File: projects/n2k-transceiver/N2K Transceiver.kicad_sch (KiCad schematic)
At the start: 131 parts, among them SW1 TS03-66-50-BK-160-LCR-D-67, SW2 TS03-66-50-BK-160-LCR-D-67, SW3 TS03-66-50-BK-160-LCR-D-67

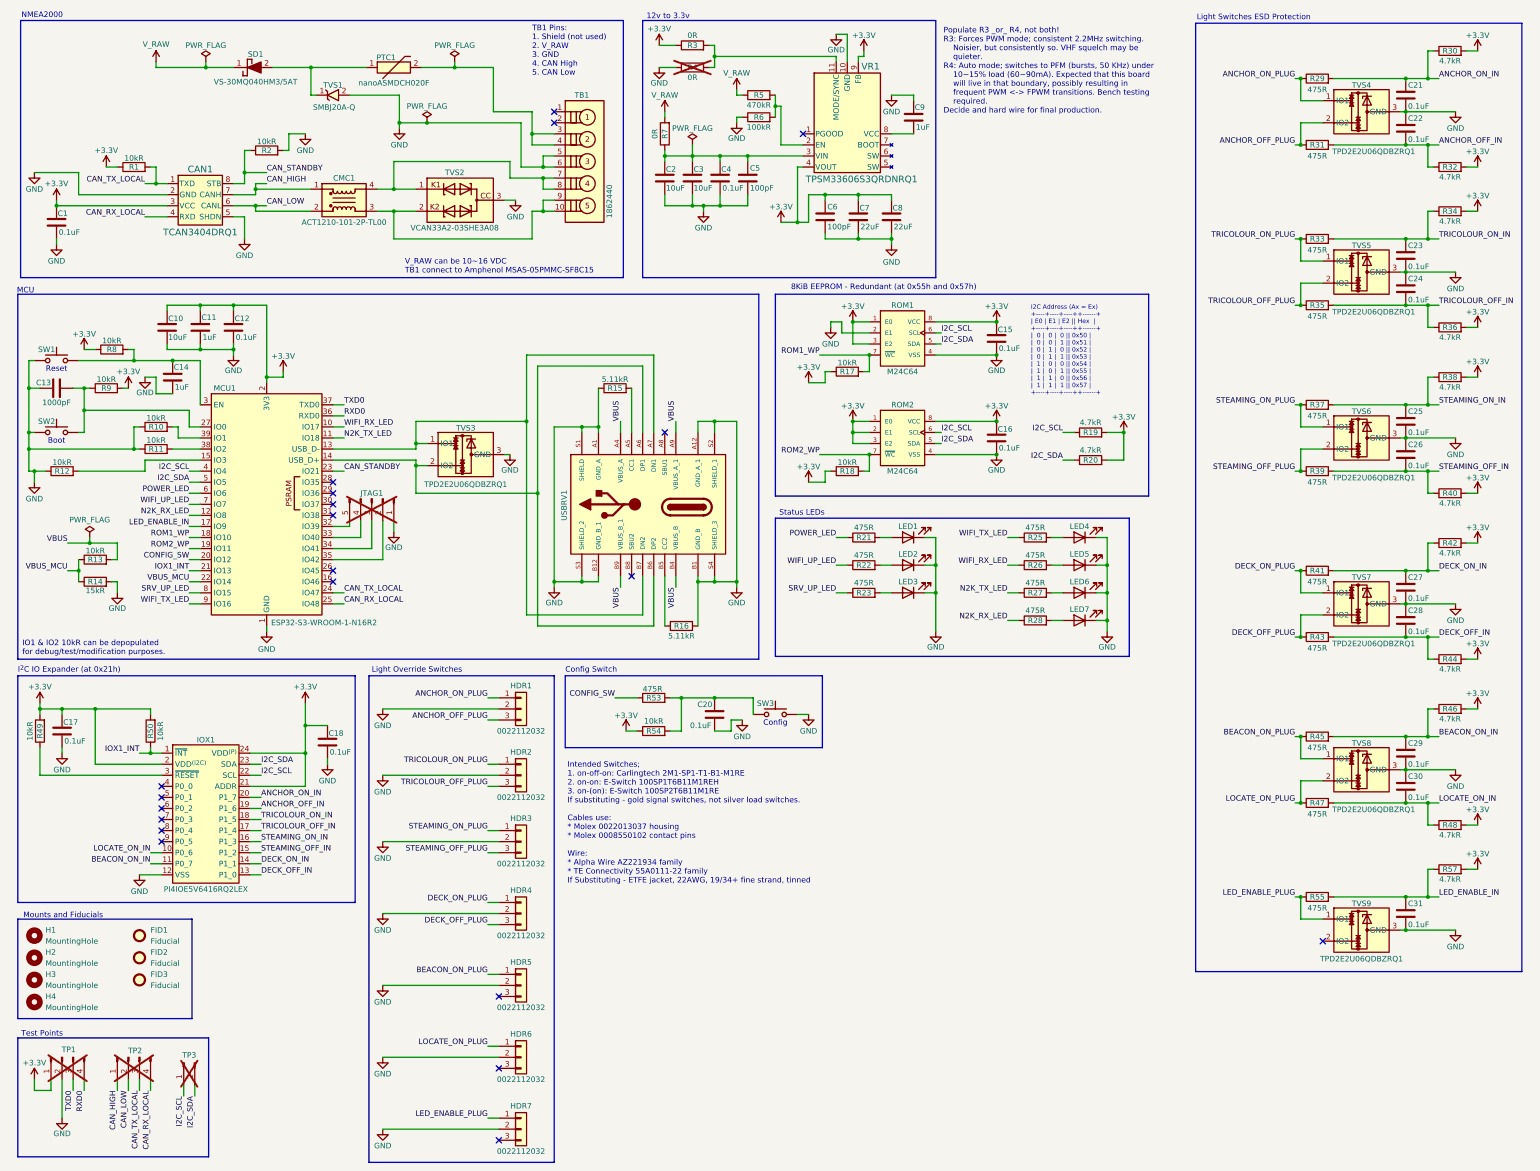
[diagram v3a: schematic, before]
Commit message: Working on switching the IOX1 to the SMI1 switch chip.
Signed-off-by: digimer <digital.mermaid@gmail.com>
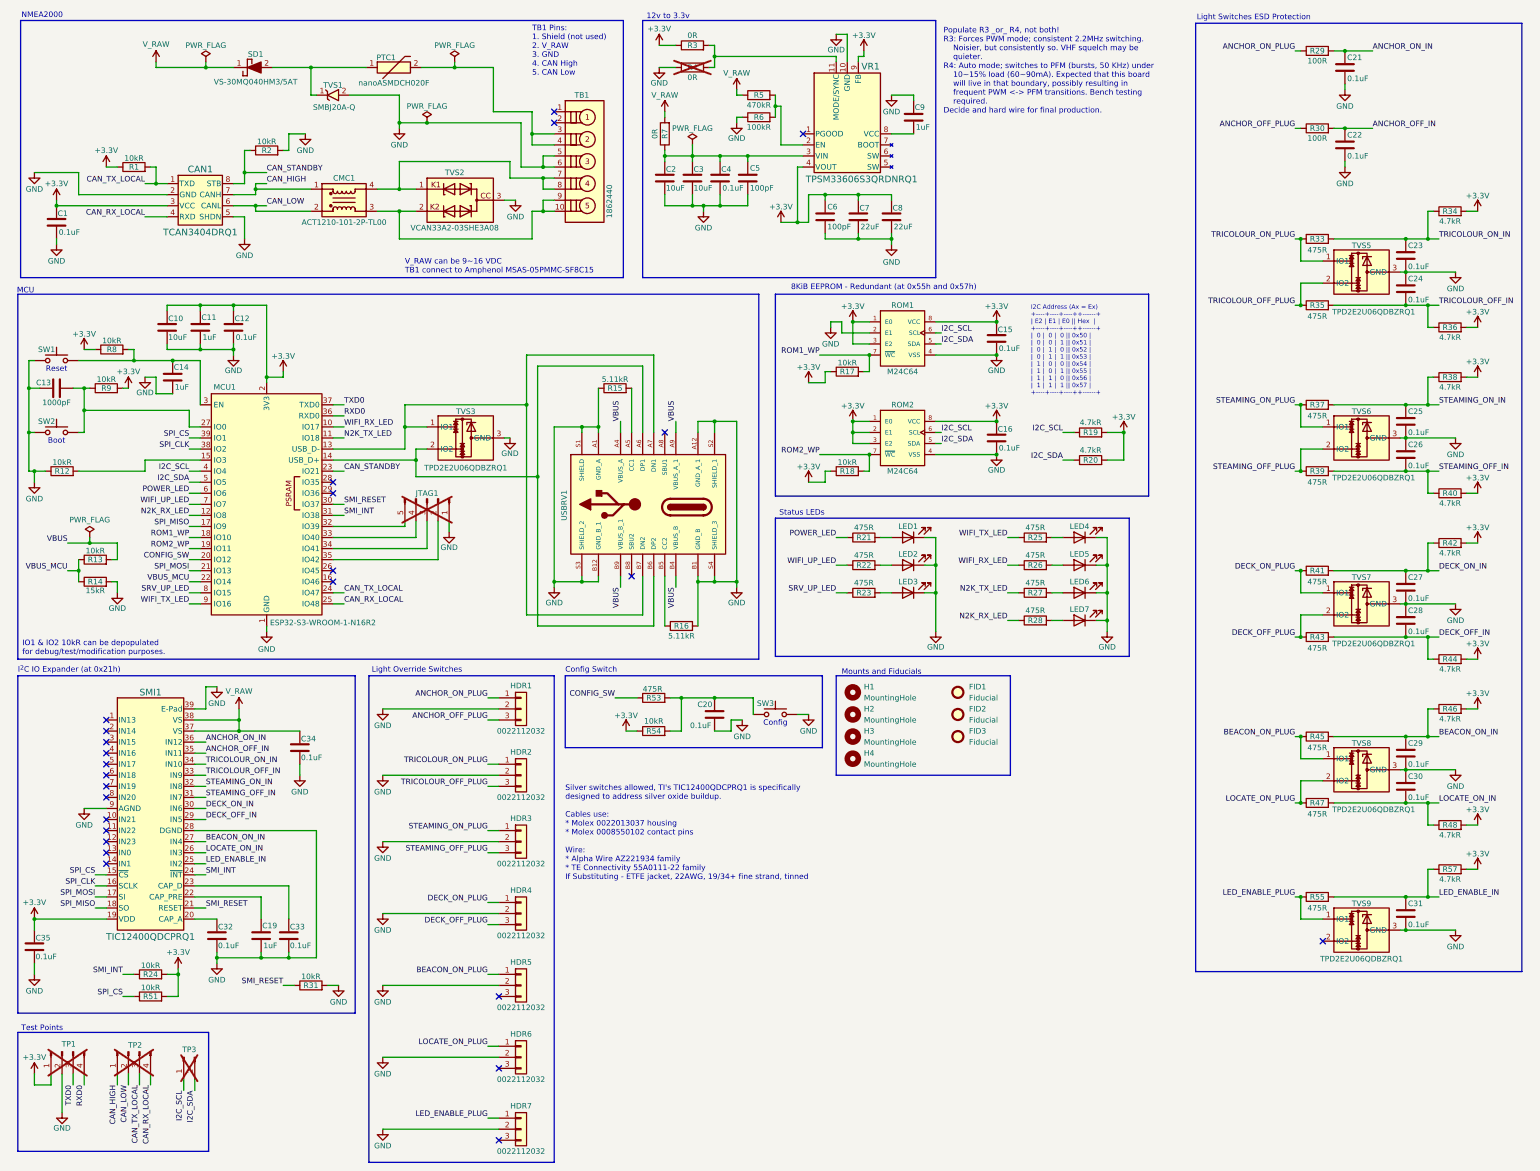
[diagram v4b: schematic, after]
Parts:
- removed C17, C18: 0.1uF, mr-stuff:Kyocera AVX 0805, symbol mr-parts:Kyocera 08051C104K4Z2A
- removed IOX1: PI4IOE5V6416RQ2LEX, mr-stuff:Diodes Inc PI4IOE5V6416RQ2LEX, symbol mr-parts:Diodes Inc PI4IOE5V6416RQ2LEX
- removed MCU1: ESP32-S3-WROOM-1-N16R2, RF_Module:ESP32-S3-WROOM-1, symbol RF_Module:ESP32-S3-WROOM-1
- removed R10, R11, R49, R50: 10kR, mr-stuff:Stackpole RNCP0805, symbol mr-parts:Stackpole RNCP0805FTD10K0
- removed R29, R31: 475R, mr-stuff:Stackpole RNCP0805, symbol mr-parts:Stackpole RNCP0805FTD475R
- removed R30, R32: 4.7kR, mr-stuff:Stackpole RMCA0805, symbol mr-parts:Stackpole RMCA0805FT4K70-HP
- removed TVS4: TPD2E2U06QDBZRQ1, mr-stuff:TI TPD2E2U06, symbol mr-parts:TVS TPD2E2U06QDBZRQ1
- added C19: 1uF, mr-stuff:Kyocera AVX 0805, symbol mr-parts:Kyocera 08051C105K4Z2A
- added C32, C33, C34, C35: 0.1uF, mr-stuff:Kyocera AVX 0805, symbol mr-parts:Kyocera 08051C104K4Z2A
- added MCU1: ESP32-S3-WROOM-1-N16R2, mr-stuff:Espressif ESP32-S3, symbol mr-parts:Espressif ESP32-S3-WROOM-1-N16R2
- added R24, R31, R51: 10kR, mr-stuff:Stackpole RNCP0805, symbol mr-parts:Stackpole RNCP0805FTD10K0
- added R29, R30: 100R, mr-stuff:Stackpole RNCP0805, symbol mr-parts:Stackpole RNCP0805FTD100R
- added SMI1: TIC12400QDCPRQ1, mr-stuff:TI TIC12400QDCPRQ1, symbol mr-parts:TI TIC12400QDCPRQ1
- C1, C12, C15, C16, C20, C21, C22, C23, C24, C25, C26, C27, C28, C29, C30, C31, C4: Datasheet2 (none) -> https://spicat.kyocera-avx.com/datasheet/08051C104K4Z2A
- C11, C14, C9: Datasheet2 (none) -> https://spicat.kyocera-avx.com/datasheet/08051C105K4Z2A
- CMC1: symbol mr-parts:TDK ACT1210-510-2P-TL00 -> mr-parts:TDK ACT1210-101-2P-TL00
- SD1: symbol mr-parts:Vishay VS-30MQ040-M3_5AT -> mr-parts:Vishay VS-30MQ040HM3/5AT
- TVS1: symbol mr-parts:Bouns SMBJ20A-Q -> mr-parts:Bourns SMBJ20A-Q
- TVS3, TVS5, TVS6, TVS7, TVS8, TVS9: symbol mr-parts:TVS TPD2E2U06QDBZRQ1 -> mr-parts:TI TPD2E2U06QDBZRQ1
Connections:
- net +3.3V: now also C35.1, MCU1.2 (3V3), R24.2, R51.2, SMI1.19 (VDD)
- net ANCHOR_OFF_IN: now also C22.1, R30.2, SMI1.35 (IN11); no longer C22.2
- net ANCHOR_OFF_PLUG: now also R30.1
- net ANCHOR_ON_IN: now also R29.2, SMI1.36 (IN12)
- net ANCHOR_ON_PLUG: now also R29.1
- net BEACON_ON_IN: now also SMI1.27 (IN4)
- net CAN_RX_LOCAL: now also MCU1.25 (IO48)
- net CAN_STANDBY: now also MCU1.23 (IO21)
- net CAN_TX_LOCAL: now also MCU1.24 (IO47)
- net CONFIG_SW: now also MCU1.20 (IO12)
- net DECK_OFF_IN: now also SMI1.29 (IN5)
- net DECK_ON_IN: now also SMI1.30 (IN6)
- net GND: now also C22.2, C19.2, C32.2, C33.2, C34.2, C35.2, MCU1.1 (GND), MCU1.40 (GND), MCU1.41 (GND), R31.2, SMI1.28 (DGND), SMI1.39 (E-Pad), SMI1.9 (AGND); no longer C22.1
- net I2C_SCL: now also MCU1.4 (IO4)
- net I2C_SDA: now also MCU1.5 (IO5)
- net LED_ENABLE_IN: now also SMI1.25 (IN2)
- net LOCATE_ON_IN: now also SMI1.26 (IN3)
- net N2K_RX_LED: now also MCU1.12 (IO8)
- net N2K_TX_LED: now also MCU1.11 (IO18)
- net POWER_LED: now also MCU1.6 (IO6)
- net ROM1_WP: now also MCU1.18 (IO10)
- net ROM2_WP: now also MCU1.19 (IO11)
- net RXD0: now also MCU1.36 (RXD0)
- net SRV_UP_LED: now also MCU1.8 (IO15)
- net STEAMING_OFF_IN: now also SMI1.31 (IN7)
- net STEAMING_ON_IN: now also SMI1.32 (IN8)
- net TRICOLOUR_OFF_IN: now also SMI1.33 (IN9)
- net TRICOLOUR_ON_IN: now also SMI1.34 (IN10)
- net TXD0: now also MCU1.37 (TXD0)
- net VBUS_MCU: now also MCU1.22 (IO14)
- net V_RAW: now also C34.1, SMI1.37 (VS), SMI1.38 (VS)
- net WIFI_RX_LED: now also MCU1.10 (IO17)
- net WIFI_TX_LED: now also MCU1.9 (IO16)
- net WIFI_UP_LED: now also MCU1.7 (IO7)
- net at C13.2, R9.1, SW2.3 (B)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: now also MCU1.27 (IO0)
- net at C14.1, R8.2, SW1.3 (B)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: now also MCU1.3 (EN)
- net at JTAG1.2 (Pin_2): now also MCU1.35 (IO42)
- net at JTAG1.3 (Pin_3): now also MCU1.34 (IO41)
- net at JTAG1.4 (Pin_4): now also MCU1.33 (IO40)
- net at JTAG1.5 (Pin_5): now also MCU1.32 (IO39)
- net at R12.2: now also MCU1.15 (IO3)
- net at TVS3.1 (IO1), USBRV1.A7 (DN1), USBRV1.B7 (DN2): now also MCU1.13 (USB_D-)
- net at TVS3.2 (IO2), USBRV1.A6 (DP1), USBRV1.B6 (DP2): now also MCU1.14 (USB_D+)
- new net: C19.1, SMI1.22 (CAP_PRE)
- new net: C32.1, SMI1.20 (CAP_A)
- new net: C33.1, SMI1.23 (CAP_D)
- new net SMI_INT: MCU1.31 (IO38), R24.1, SMI1.24 (~{INT})
- new net SMI_RESET: MCU1.30 (IO37), R31.1, SMI1.21 (RESET)
- new net SPI_CLK: MCU1.38 (IO2), SMI1.16 (SCLK)
- new net SPI_CS: MCU1.39 (IO1), R51.1, SMI1.15 (~{CS})
- new net SPI_MISO: MCU1.17 (IO9), SMI1.18 (SO)
- new net SPI_MOSI: MCU1.21 (IO13), SMI1.17 (SI)
- no-connect marks 21 -> 26
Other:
- note added: "I2C Address (Ax = Ex) +----+----+----++------+ | E2 | E1 | E0 || Hex | +----+----+----++------+ | 0 | 0 | 0 || 0x50 | | 0 | 0 | 1 || 0x51 | | 0 | 1 | 0 || 0x52 | | 0 | 1 | 1 || 0x53 | | 1 | 0 | 0 || 0x54 | | 1 | 0 | 1 || 0x55 | | 1 | 1 | 0 || 0x56 | | 1 | 1 | 1 || 0x57 | +----+----+----++------+"
- note added: "Populate R3 _or_ R4, not both! R3: Forces PWM mode; consistent 2.2MHz switching. Noisier, but consistently so. VHF squelch may be quieter. R4: Auto mode; switches to PFM (bursts, 50 KHz) under 10~15% load (60~90mA). Expected that this board will live in that boundary, possibly resulting in frequent PWM <-> PFM transitions. Bench testing required. Decide and hard wire for final production."
- note added: "Silver switches allowed, TI's TIC12400QDCPRQ1 is specifically designed to address silver oxide buildup. Cables use: * Molex 0022013037 housing * Molex 0008550102 contact pins Wire: * Alpha Wire AZ221934 family * TE Connectivity 55A0111-22 family If Substituting - ETFE jacket, 22AWG, 19/34+ fine strand, tinned"
- note added: "V_RAW can be 9~16 VDC TB1 connect to Amphenol MSAS-05PMMC-SF8C15"
- note removed: "I2C Address (Ax = Ex) +----+----+----++------+ | E0 | E1 | E2 || Hex | +----+----+----++------+ | 0 | 0 | 0 || 0x50 | | 0 | 0 | 1 || 0x51 | | 0 | 1 | 0 || 0x52 | | 0 | 1 | 1 || 0x53 | | 1 | 0 | 0 || 0x54 | | 1 | 0 | 1 || 0x55 | | 1 | 1 | 0 || 0x56 | | 1 | 1 | 1 || 0x57 | +----+----+----++------+"
- note removed: "Intended Switches; 1. on-off-on: Carlingtech 2M1-SP1-T1-B1-M1RE 2. on-on: E-Switch 100SP1T6B11M1REH 3. on-(on): E-Switch 100SP2T6B11M1RE If substituting - gold signal switches, not silver load switches. Cables use: * Molex 0022013037 housing * Molex 0008550102 contact pins Wire: * Alpha Wire AZ221934 family * TE Connectivity 55A0111-22 family If Substituting - ETFE jacket, 22AWG, 19/34+ fine stra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"
- note removed: "Populate R3 _or_ R4, not both! R3: Forces PWM mode; consistent 2.2MHz switching. Noisier, but consistently so. VHF squelch may be quieter. R4: Auto mode; switches to PFM (bursts, 50 KHz) under 10~15% load (60~90mA). Expected that this board will live in that boundary, possibly resulting in frequent PWM <-> FPWM transitions. Bench testing required. Decide and hard wire for final production."
- note removed: "V_RAW can be 10~16 VDC TB1 connect to Amphenol MSAS-05PMMC-SF8C15"
- moved on the sheet: C21, C22, FID1, FID2, FID3, H1, H2, H3, H4, JTAG1, TP1, TP2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

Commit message: Finished the schematic update to use the SMI1.
Also updated the ESD protection to account for the TIC12400QDCPRQ1's internal ESD functions.

Signed-off-by: digimer <digital.mermaid@gmail.com>
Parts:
- removed C23, C24, C25, C26, C27, C28, C29, C30, C31: 0.1uF, mr-stuff:Kyocera AVX 0805, symbol mr-parts:Kyocera 08051C104K4Z2A
- removed R33, R35, R37, R39, R41, R43, R45, R47, R55: 475R, mr-stuff:Stackpole RNCP0805, symbol mr-parts:Stackpole RNCP0805FTD475R
- removed R34, R36, R38, R40, R42, R44, R46, R48, R57: 4.7kR, mr-stuff:Stackpole RMCA0805, symbol mr-parts:Stackpole RMCA0805FT4K70-HP
- removed TVS5, TVS6, TVS7, TVS8, TVS9: TPD2E2U06QDBZRQ1, mr-stuff:TI TPD2E2U06, symbol mr-parts:TI TPD2E2U06QDBZRQ1
- added C36, C37, C38, C39, C40, C41, C42, C43, C44: 0.1uF, mr-stuff:Kyocera AVX 0805, symbol mr-parts:Kyocera 08051C104K4Z2A
- added R33, R35, R37, R39, R41, R43, R45, R47, R55: 100R, mr-stuff:Stackpole RNCP0805, symbol mr-parts:Stackpole RNCP0805FTD100R
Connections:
- net BEACON_ON_IN: now also C42.1, R45.2
- net BEACON_ON_PLUG: now also R45.1
- net DECK_OFF_IN: now also C41.1, R43.2
- net DECK_OFF_PLUG: now also R43.1
- net DECK_ON_IN: now also C40.1, R41.2
- net DECK_ON_PLUG: now also R41.1
- net GND: now also C36.2, C37.2, C38.2, C39.2, C40.2, C41.2, C42.2, C43.2, C44.2
- net LED_ENABLE_IN: now also C44.1, R55.2
- net LED_ENABLE_PLUG: now also R55.1
- net LOCATE_ON_IN: now also C43.1, R47.2
- net LOCATE_ON_PLUG: now also R47.1
- net STEAMING_OFF_IN: now also C39.1, R39.2
- net STEAMING_OFF_PLUG: now also R39.1
- net STEAMING_ON_IN: now also C38.1, R37.2
- net STEAMING_ON_PLUG: now also R37.1
- net TRICOLOUR_OFF_IN: now also C37.1, R35.2
- net TRICOLOUR_OFF_PLUG: now also R35.1
- net TRICOLOUR_ON_IN: now also C36.1, R33.2
- net TRICOLOUR_ON_PLUG: now also R33.1
- no-connect marks 26 -> 25
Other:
- note removed: "IO1 & IO2 10kR can be depopulated for debug/test/modification purposes."

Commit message: Added the new N2K Breakwater PCB.
This is a general purpose NMEA2000 protection board designed to be used across all projects connected to the NMEA2000 bus. It is designed to survive high voltage transients caused by conditions like an alternator dump, large inductive load transients, etc.

Signed-off-by: digimer <digital.mermaid@gmail.com>
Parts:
- added C34: 3300pF, mr-stuff:TDK CGA 0805, symbol mr-parts:TDK CGA3E1C0G2A332J080AE
- added C35: 1uF, mr-stuff:Kyocera AVX 0805, symbol mr-parts:Kyocera 08051C105K4Z2A
- added PMIC1: LTC4368HMS-2#WPBF, mr-stuff:ADI LTC4368, symbol mr-parts:ADI LTC4368HMS-2#WPBF
- added Q1, Q2: SQJ872EP-T1_BE3, mr-stuff:Vishay SQJ872EP, symbol mr-parts:Vishay SQJ872EP-T1_BE3
- added R29: 10kR, mr-stuff:Stackpole RNCP0805, symbol mr-parts:Stackpole RNCP0805FTD10K0
- added R43: 22.1kR, mr-stuff:Stackpole RNCP0805, symbol mr-parts:Stackpole RNCP0805FTD22K1
- added R44: 0.05R, mr-stuff:Vishay WSLP 1206 4-wire Kelvin, symbol mr-parts:Vishay WSLP1206R0500FEA
- renumbered C34 to C17, C35 to C18, C32 to C19, C19 to C20, C33 to C21, C20 to C22, C21 to C23, C22 to C24, C36 to C25, C37 to C26, C38 to C27, C39 to C28, C40 to C29, C41 to C30, C42 to C31, C43 to C32, C44 to C33, R12 to R10, R13 to R11, R14 to R12, R15 to R13, R16 to R14, R17 to R15, R18 to R16, R19 to R17, R20 to R18, R21 to R19, R22 to R20, R23 to R21, R25 to R22, R26 to R23, R27 to R24, R28 to R25, R24 to R26, R51 to R27, R31 to R28, R53 to R30, R54 to R31, R29 to R32, R30 to R33, R33 to R34, R37 to R36, R39 to R37, R41 to R38, R43 to R39, R45 to R40, R47 to R41, R55 to R42
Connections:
- net GND: now also C34.2, C35.2, R29.2
- net SPI_CLK: now also R29.1
- net V_RAW: now also PTC1.2, TB1.3, TB1.4, PMIC1.1 (VIN), Q1.5 (D); no longer C17.1, R5.1, R7.2, SD1.1 (K), SMI1.37 (VS), SMI1.38 (VS)
- new net: Q1.1 (S), Q1.2 (S), Q1.3 (S), Q2.1 (S), Q2.2 (S), Q2.3 (S)
- new net: C34.1, R43.2
- new net PMIC_GATE: PMIC1.10 (GATE), Q1.4 (G), Q2.4 (G), R43.1
- new net PMIC_SENSE: PMIC1.9 (SENSE), Q2.5 (D), R44.1, R44.3
- new net V_OUT: C17.1, C35.1, PMIC1.8 (VOUT), R44.2, R44.4, R5.1, R7.2, SD1.1 (K), SMI1.37 (VS), SMI1.38 (VS)
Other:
- note added: "Multiple Switch Detection Interface"
- note added: "Silver switches allowed, TI's TIC12400QDCPRQ1 is specifically designed to address silver oxide buildup. Switches: * on-off-on: Carlingtech 2M1-SP3-T6-B1-M1QE * Anchor Light * Tricolour Light * Steaming Light * Deck Light * on-on: Carlingtech 2M1-SP1-T6-B1-M1QE * Beacon Mode * Locate Mode * on-mom: Carlingtech 2M1-SP2-T6-B1-M1QE * Status LEDs (possibly on-on, TBD) Cables: * Molex 0022013037 housin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"
- note added: "ToDo: Switch to LTC4368HMS-2#WPBF, replace PTC, add SMD fuse"
- note removed: "I^{2}C IO Expander (at 0x21h)"
- note removed: "Silver switches allowed, TI's TIC12400QDCPRQ1 is specifically designed to address silver oxide buildup. Cables use: * Molex 0022013037 housing * Molex 0008550102 contact pins Wire: * Alpha Wire AZ221934 family * TE Connectivity 55A0111-22 family If Substituting - ETFE jacket, 22AWG, 19/34+ fine strand, tinned"
- moved on the sheet: R26, R27, R28, TP1, TP2, TP3
